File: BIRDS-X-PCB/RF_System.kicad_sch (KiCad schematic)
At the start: 37 parts, among them J501 60611002111501, J502 Conn_01x12, Q501 2N7002, Q502 2N7002, U1 MCP6004T-I/ST, U503 DRA818V

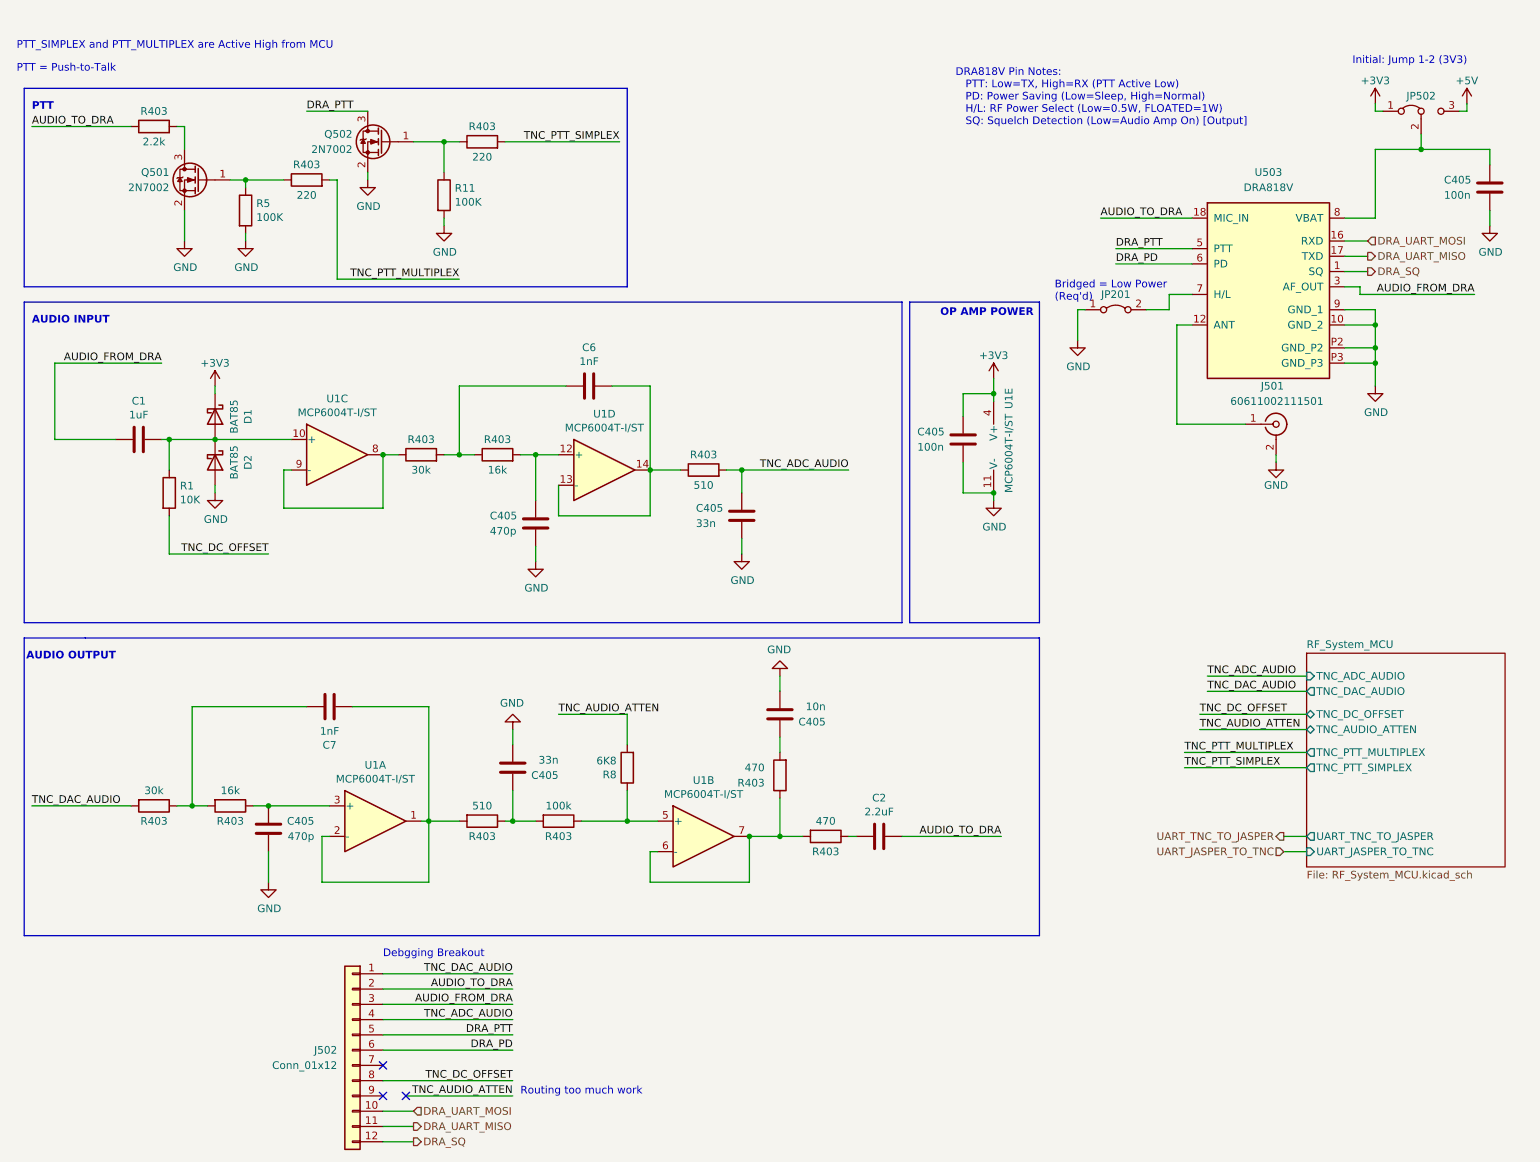
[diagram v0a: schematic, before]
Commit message: Update to new STM32F103 MCU
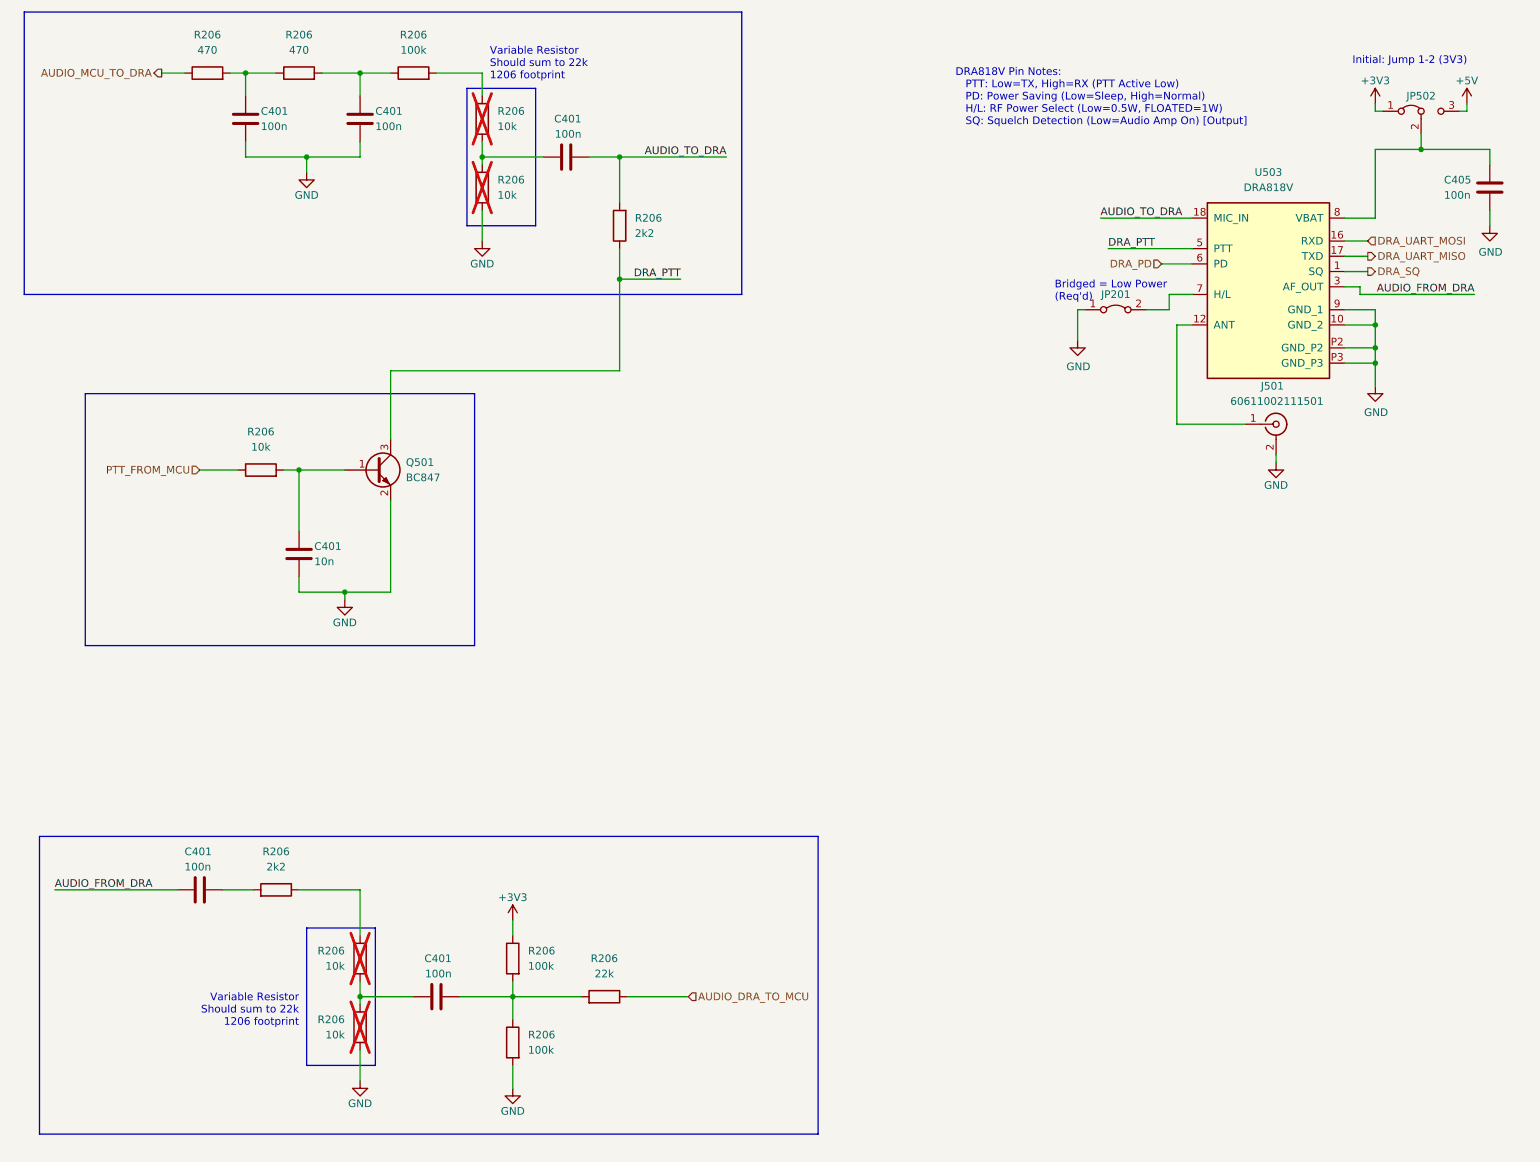
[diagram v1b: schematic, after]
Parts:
- removed C1: 1uF, Capacitor_SMD:C_0603_1608Metric_Pad1.08x0.95mm_HandSolder, symbol Device:C
- removed C2: 2.2uF, Capacitor_SMD:C_0603_1608Metric_Pad1.08x0.95mm_HandSolder, symbol Device:C
- removed C405 (x2): 33n, Capacitor_SMD:C_0603_1608Metric_Pad1.08x0.95mm_HandSolder, symbol Device:C
- removed C405: 100n, Capacitor_SMD:C_0603_1608Metric_Pad1.08x0.95mm_HandSolder, symbol Device:C
- removed C405: 10n, Capacitor_SMD:C_0603_1608Metric_Pad1.08x0.95mm_HandSolder, symbol Device:C
- removed C405 (x2): 470p, Capacitor_SMD:C_0603_1608Metric_Pad1.08x0.95mm_HandSolder, symbol Device:C
- removed C6, C7: 1nF, Capacitor_SMD:C_0603_1608Metric_Pad1.08x0.95mm_HandSolder, symbol Device:C
- removed D1, D2: BAT85, Diode_THT:D_DO-35_SOD27_P7.62mm_Horizontal, symbol Diode:BAT85
- removed J502: Conn_01x12, Connector_PinHeader_1.27mm:PinHeader_1x12_P1.27mm_Vertical, symbol Connector_Generic:Conn_01x12
- removed Q501, Q502: 2N7002, Package_TO_SOT_SMD:SOT-23, symbol Transistor_FET:2N7002
- removed R1: 10K, Resistor_SMD:R_0603_1608Metric_Pad0.98x0.95mm_HandSolder, symbol Device:R
- removed R11, R5: 100K, Resistor_SMD:R_0603_1608Metric_Pad0.98x0.95mm_HandSolder, symbol Device:R
- removed R403 (x2): 30k, Resistor_SMD:R_0603_1608Metric_Pad0.98x0.95mm_HandSolder, symbol Device:R
- removed R403 (x2): 470, Resistor_SMD:R_0603_1608Metric_Pad0.98x0.95mm_HandSolder, symbol Device:R
- removed R403 (x2): 510, Resistor_SMD:R_0603_1608Metric_Pad0.98x0.95mm_HandSolder, symbol Device:R
- removed R403 (x2): 16k, Resistor_SMD:R_0603_1608Metric_Pad0.98x0.95mm_HandSolder, symbol Device:R
- removed R403: 100k, Resistor_SMD:R_0603_1608Metric_Pad0.98x0.95mm_HandSolder, symbol Device:R
- removed R403: 2.2k, Resistor_SMD:R_0603_1608Metric_Pad0.98x0.95mm_HandSolder, symbol Device:R
- removed R403 (x2): 220, Resistor_SMD:R_0603_1608Metric_Pad0.98x0.95mm_HandSolder, symbol Device:R
- removed R8: 6K8, Resistor_SMD:R_0603_1608Metric_Pad0.98x0.95mm_HandSolder, symbol Device:R
- removed U1: MCP6004T-I/ST, Package_SO:TSSOP-14_4.4x5mm_P0.65mm, symbol Amplifier_Operational:MCP6004
- added C401: 10n, Capacitor_SMD:C_0603_1608Metric_Pad1.08x0.95mm_HandSolder, symbol Device:C
- added C401 (x5): 100n, Capacitor_SMD:C_0603_1608Metric_Pad1.08x0.95mm_HandSolder, symbol Device:C
- added Q501: BC847, Package_TO_SOT_SMD:SOT-23, symbol Transistor_BJT:BC847
- added R206 (x2): 2k2, Resistor_SMD:R_0603_1608Metric_Pad0.98x0.95mm_HandSolder, symbol Device:R
- added R206: 10k, Resistor_SMD:R_0603_1608Metric_Pad0.98x0.95mm_HandSolder, symbol Device:R
- added R206 (x2): 470, Resistor_SMD:R_0603_1608Metric_Pad0.98x0.95mm_HandSolder, symbol Device:R
- added R206 (x3): 100k, Resistor_SMD:R_0603_1608Metric_Pad0.98x0.95mm_HandSolder, symbol Device:R
- added R206 (x4): 10k, Resistor_SMD:R_1206_3216Metric_Pad1.30x1.75mm_HandSolder, symbol Device:R
- added R206: 22k, Resistor_SMD:R_0603_1608Metric_Pad0.98x0.95mm_HandSolder, symbol Device:R
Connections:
- net +3V3: now also R206.1
- net AUDIO_FROM_DRA: now also C401.2
- net AUDIO_TO_DRA: now also C401.2, R206.2
- net DRA_PTT: now also Q501.3 (C), R206.1
- net GND: now also C401.2, C401.2, C401.2, Q501.2 (E), R206.1, R206.1, R206.2
- new net: C401.1, Q501.1 (B), R206.2
- new net: C401.1, R206.1, R206.2 (x4)
- new net: C401.2, R206.1, R206.2, R206.2
- new net: R206.1, R206.2
- new net: C401.1, R206.2
- new net: R206.2, R206.2
- new net AUDIO_DRA_TO_MCU: R206.1
- new net AUDIO_MCU_TO_DRA: R206.1
- new net PTT_FROM_MCU: R206.1
- no-connect marks 3 -> 0
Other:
- removed sheet RF_System_MCU
- note added: "Variable Resistor Should sum to 22k 1206 footprint"
- note removed: "AUDIO INPUT"
- note removed: "AUDIO OUTPUT"
- note removed: "Debgging Breakout"
- note removed: "OP AMP POWER"
- note removed: "PTT"
- note removed: "PTT = Push-to-Talk"
- note removed: "PTT_SIMPLEX and PTT_MULTIPLEX are Active High from MCU"
- note removed: "Routing too much work"

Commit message: Prep docs for Rev5.1 release
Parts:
- R206: now not fitted
- R206: value 2k2 -> 0
- R206: now fitted
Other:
- note added: "PTT Inverter"
- note added: "Rev5.1: Close JP501"
- note added: "Rev5.1: DNP"
- note added: "Rev5.1: Jump 1-2 (3V3)"
- note added: "Rev5.1: R511 = 0 ohms"
- note added: "Variable Resistor. Should sum to 22k. 1206 footprint."
- note removed: "Initial: Jump 1-2 (3V3)"
- note removed: "Variable Resistor Should sum to 22k 1206 footprint"
- moved on the sheet: C401, Q501, R206

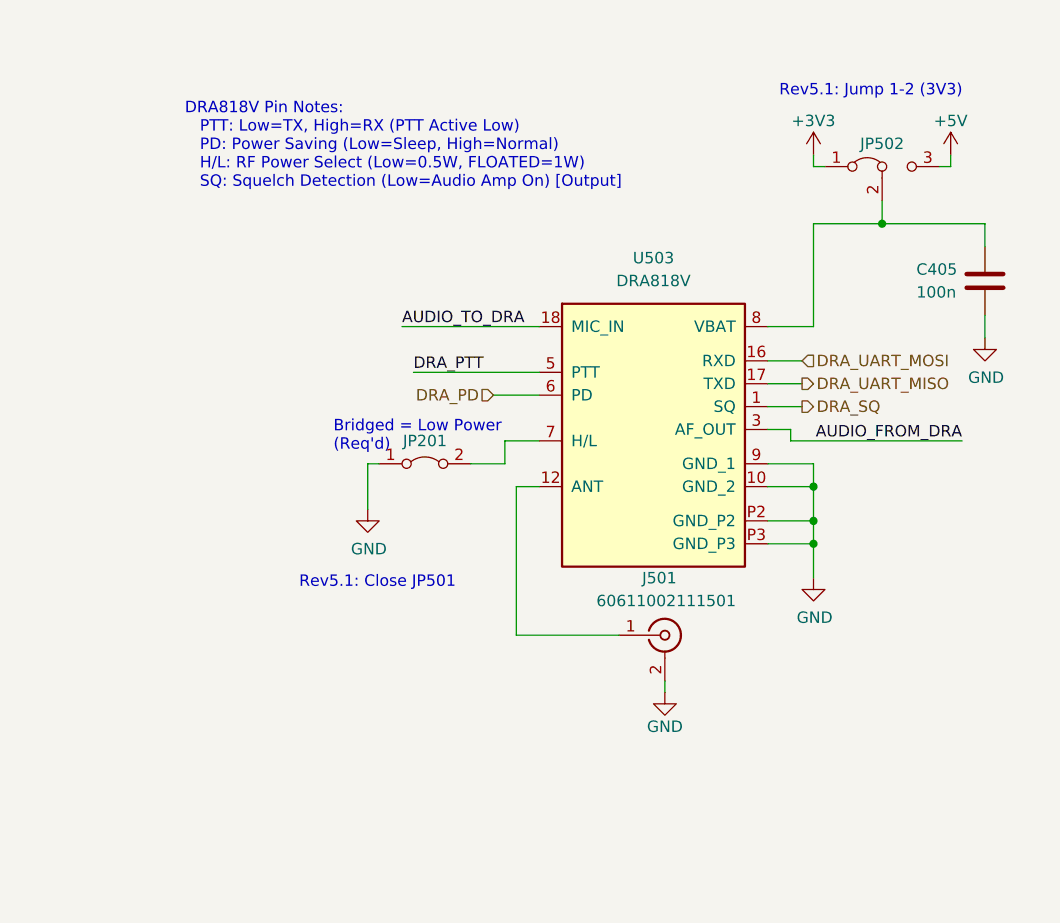
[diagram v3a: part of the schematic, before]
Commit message: Update schematics with LinearCCDs, remove flash
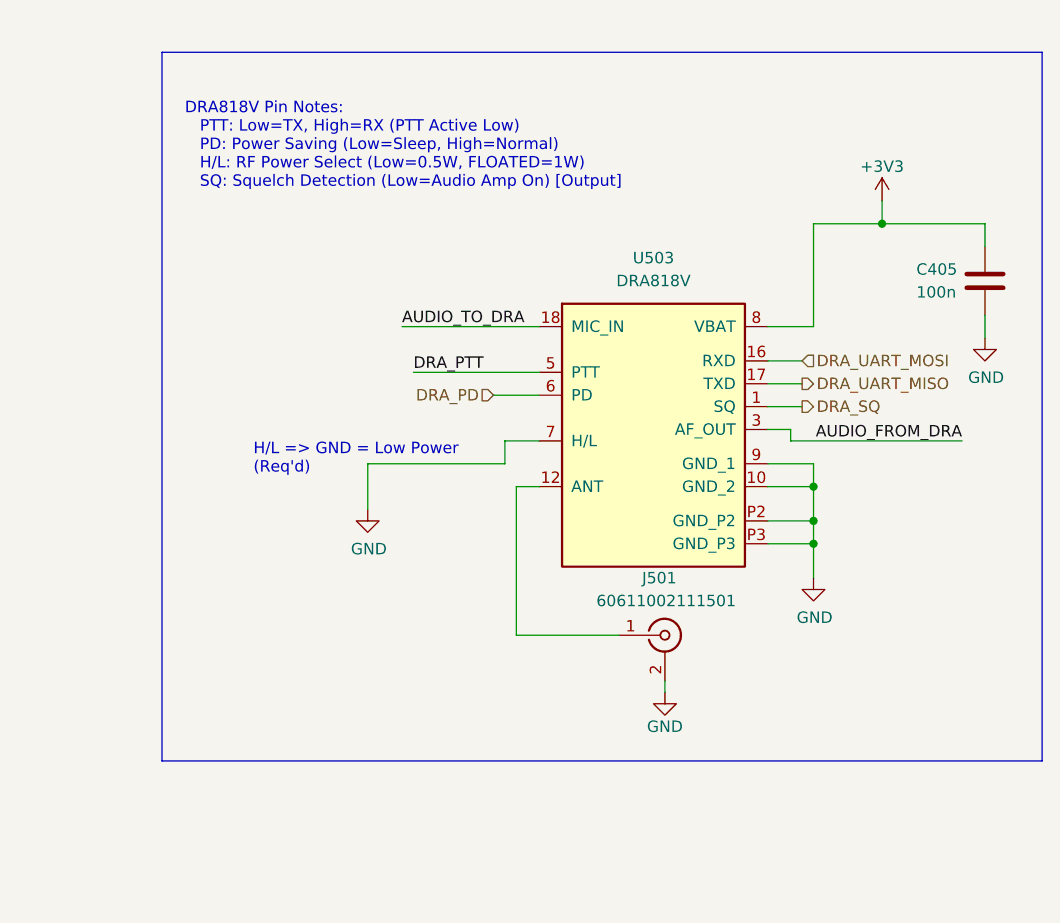
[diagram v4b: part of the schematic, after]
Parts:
- removed JP201: Jumper_2_Open, Jumper:SolderJumper-2_P1.3mm_Open_RoundedPad1.0x1.5mm, symbol Jumper:Jumper_2_Bridged
- removed JP502: Jumper_3_Bridged12, Jumper:SolderJumper-3_P1.3mm_Open_RoundedPad1.0x1.5mm_NumberLabels, symbol Jumper:Jumper_3_Bridged12
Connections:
- net +3V3: now also C405.1, U503.8 (VBAT)
- net GND: now also U503.7 (H/L)
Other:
- note added: "H/L => GND = Low Power (Req'd)"
- note removed: "Bridged = Low Power (Req'd)"
- note removed: "Rev5.1: Close JP501"
- note removed: "Rev5.1: Jump 1-2 (3V3)"
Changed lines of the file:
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@@
     (stroke (width 0) (type default))
   )
-  (wire (pts (xy 201.93 62.23) (xy 205.74 62.23))
-    (stroke (width 0) (type default))
-  )
-  (wire (pts (xy 190.5 62.23) (xy 191.77 62.23))
+  (wire (pts (xy 190.5 62.23) (xy 205.74 62.23))
     (stroke (width 0) (type default))
   )
@@
     (stroke (width 0) (type default))
   )
-  (wire (pts (xy 240.03 29.21) (xy 240.03 27.94))
-    (stroke (width 0) (type default))
-  )
   (wire (pts (xy 234.95 68.58) (xy 240.03 68.58))
     (stroke (width 0) (type default))
   )
-  (wire (pts (xy 255.27 27.94) (xy 255.27 29.21))
-    (stroke (width 0) (type default))
-  )
   (wire (pts (xy 93.98 134.62) (xy 93.98 138.43))
     (stroke (width 0) (type default))
@@
     (stroke (width 0) (type default))
   )
-  (wire (pts (xy 255.27 29.21) (xy 254 29.21))
-    (stroke (width 0) (type default))
-  )
-  (wire (pts (xy 241.3 29.21) (xy 240.03 29.21))
-    (stroke (width 0) (type default))
-  )
   (wire (pts (xy 234.95 46.99) (xy 240.03 46.99))
     (stroke (width 0) (type default))
@@
   )
   (rectangle (start 59.69 146.05) (end 71.12 123.19)
+    (stroke (width 0) (type default))
+    (fill (type none))
+  )
+  (rectangle (start 167.64 16.51) (end 265.43 95.25)
     (stroke (width 0) (type default))
     (fill (type none))
@@
     (effects (font (size 1.27 1.27)) (justify right bottom))
   )
-  (text "Bridged = Low Power\n(Req'd)" (at 186.69 60.96 0)
+  (text "H/L => GND = Low Power\n(Req'd)" (at 177.8 63.5 0)
     (effects (font (size 1.27 1.27)) (justify left bottom))
   )
   (text "PTT Inverter" (at 26.67 67.31 0)
-    (effects (font (size 1.27 1.27)) (justify left bottom))
-  )
-  (text "Rev5.1: Close JP501" (at 182.88 76.2 0)
     (effects (font (size 1.27 1.27)) (justify left bottom))
   )
@@
   )
   (text "Rev5.1: DNP" (at 80.01 50.8 0)
-    (effects (font (size 1.27 1.27)) (justify left bottom))
-  )
-  (text "Rev5.1: Jump 1-2 (3V3)" (at 236.22 21.59 0)
     (effects (font (size 1.27 1.27)) (justify left bottom))
   )
@@
     )
   )
-  (symbol (lib_id "power:+5V") (at 255.27 27.94 0) (unit 1)
-    (in_bom yes) (on_board yes) (dnp no)
-    (property "Reference" "#PWR0516" (at 255.27 31.75 0)
-      (effects (font (size 1.27 1.27)) hide)
-    )
-    (property "Value" "+5V" (at 255.27 24.13 0)
-      (effects (font (size 1.27 1.27)))
-    )
-    (property "Footprint" "" (at 255.27 27.94 0)
-      (effects (font (size 1.27 1.27)) hide)
-    )
-    (property "Datasheet" "" (at 255.27 27.94 0)
-      (effects (font (size 1.27 1.27)) hide)
-    )
-    (pin "1")
-    (instances
-      (project "BIRDS-X-PCB"
-        (path "/c2796b15-795a-4d6e-ad4b-0ba87ded4bc9/245c031a-1c72-4f7a-bf07-271990525459"
-          (reference "#PWR0516") (unit 1)
-        )
-      )
-    )
-  )
   (symbol (lib_id "power:GND") (at 68.58 148.59 0) (mirror y) (unit 1)
     (in_bom yes) (on_board yes) (dnp no)
@@
     )
   )
-  (symbol (lib_id "Jumper:Jumper_3_Bridged12") (at 247.65 29.21 0) (unit 1)
-    (in_bom yes) (on_board yes) (dnp no)
-    (property "Reference" "JP502" (at 247.65 26.67 0)
-      (effects (font (size 1.27 1.27)))
-    )
-    (property "Value" "Jumper_3_Bridged12" (at 247.65 25.4 0)
-      (effects (font (size 1.27 1.27)) hide)
-    )
-    (property "Footprint" "Jumper:SolderJumper-3_P1.3mm_Open_RoundedPad1.0x1.5mm_NumberLabels" (at 247.65 29.21 0)
-      (effects (font (size 1.27 1.27)) hide)
-    )
-    (property "Datasheet" "~" (at 247.65 29.21 0)
-      (effects (font (size 1.27 1.27)) hide)
-    )
-    (pin "1")
-    (pin "2")
-    (pin "3")
-    (instances
-      (project "BIRDS-X-PCB"
-        (path "/c2796b15-795a-4d6e-ad4b-0ba87ded4bc9/245c031a-1c72-4f7a-bf07-271990525459"
-          (reference "JP502") (unit 1)
-        )
-      )
-    )
-  )
   (symbol (lib_id "Device:R") (at 93.98 142.24 0) (mirror y) (unit 1)
     (in_bom yes) (on_board yes) (dnp no) (fields_autoplaced)
@@
     )
   )
-  (symbol (lib_id "power:+3V3") (at 240.03 27.94 0) (unit 1)
-    (in_bom yes) (on_board yes) (dnp no) (fields_autoplaced)
-    (property "Reference" "#PWR0408" (at 240.03 31.75 0)
-      (effects (font (size 1.27 1.27)) hide)
-    )
-    (property "Value" "+3V3" (at 240.03 24.13 0)
-      (effects (font (size 1.27 1.27)))
-    )
-    (property "Footprint" "" (at 240.03 27.94 0)
-      (effects (font (size 1.27 1.27)) hide)
-    )
-    (property "Datasheet" "" (at 240.03 27.94 0)
+  (symbol (lib_id "power:+3V3") (at 247.65 33.02 0) (unit 1)
+    (in_bom yes) (on_board yes) (dnp no) (fields_autoplaced)
+    (property "Reference" "#PWR0408" (at 247.65 36.83 0)
+      (effects (font (size 1.27 1.27)) hide)
+    )
+    (property "Value" "+3V3" (at 247.65 29.21 0)
+      (effects (font (size 1.27 1.27)))
+    )
+    (property "Footprint" "" (at 247.65 33.02 0)
+      (effects (font (size 1.27 1.27)) hide)
+    )
+    (property "Datasheet" "" (at 247.65 33.02 0)
       (effects (font (size 1.27 1.27)) hide)
     )
@@
         )
       )
-    )
-  )
-  (symbol (lib_id "Jumper:Jumper_2_Bridged") (at 196.85 62.23 0) (unit 1)
-    (in_bom yes) (on_board yes) (dnp no)
-    (property "Reference" "JP201" (at 196.85 59.69 0)
-      (effects (font (size 1.27 1.27)))
-    )
-    (property "Value" "Jumper_2_Open" (at 194.945 63.5 90)
-      (effects (font (size 1.27 1.27)) (justify right) hide)
-    )
-    (property "Footprint" "Jumper:SolderJumper-2_P1.3mm_Open_RoundedPad1.0x1.5mm" (at 196.85 62.23 0)
-      (effects (font (size 1.27 1.27)) hide)
-    )
-    (property "Datasheet" "~" (at 196.85 62.23 0)
-      (effects (font (size 1.27 1.27)) hide)
-    )
-    (pin "1")
-    (pin "2")
-    (instances
-      (project "BIRDS-X-PCB"
-        (path "/c2796b15-795a-4d6e-ad4b-0ba87ded4bc9/f0b1214b-f453-423f-b2cf-f5d10e08eafe"
-          (reference "JP201") (unit 1)
-        )
-        (path "/c2796b15-795a-4d6e-ad4b-0ba87ded4bc9/245c031a-1c72-4f7a-bf07-271990525459"
-          (reference "JP501") (unit 1)
-        )
-      )
